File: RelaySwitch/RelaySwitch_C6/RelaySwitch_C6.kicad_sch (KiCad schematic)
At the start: 39 parts, among them J1 AC_MAINS_IN, J3 LOAD_CH1, J4 LOAD_CH2, J5 SW1_INPUT, J6 SW2_INPUT, K1 G5Q-1-DC5, K2 G5Q-1-DC5, Q1 MMBT8050, Q2 MMBT8050, U1 HLK-2M05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

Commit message: 07/03
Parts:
- removed R10: 1m, Resistor_SMD:R_2512_6332Metric, symbol Device:R
- added C2: 10u, Capacitor_SMD:C_0402_1005Metric, symbol Device:C_Small
- added C3: 100n, Capacitor_SMD:C_0402_1005Metric, symbol Device:C_Small
- R18: footprint Resistor_SMD:R_Shunt_Vishay_WSK2512_6332Metric_T2.66mm -> XIAO_Series_Footprints:RES_WSK2512R0100FEA; symbol Device:R -> WSK2512R0100FEA:WSK2512R0100FEA; Check_prices (none) -> https://www.snapeda.com/parts/WSK2512R0100FEA/Vishay/view-p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; Description_1 (none) -> Metal Strip Low Ohmic Smnt Resistor 2512 Case 10mOhm +/-1% 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; DigiKey_Part_Number (none) -> 541-WSK2512R0100FEACT-ND; MANUFACTURER (none) -> Vishay Dale; MAXIMUM_PACKAGE_HEIGHT (none) -> 0.889mm; MF (none) -> Vishay; MP (none) -> WSK2512R0100FEA; PARTREV (none) -> 04-Apr-2022; Package (none) -> None; SNAPEDA_PN (none) -> WSK2512R0100FEA; STANDARD (none) -> Manufacturer Recommendations; SnapEDA_Link (none) -> https://www.snapeda.com/parts/WSK2512R0100FEA/Vishay/view-p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
- U2: footprint XIAO_Series_Footprints:XIAO-ESP32-C6-SMD -> XIAO_Series_Footprints:XIAO-ESP32-C6-DIP
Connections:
- net +3V3: now also C3.1; no longer C5.1
- net +5V: now also C5.1, C2.1
- net GND: now also U5.4 (V2P), C2.2, C3.2; no longer U5.3 (V1N)
- net L: now also R18.I1; no longer R18.1, U5.4 (V2P)
- net L_Sense: now also R18.I2; no longer R18.2
- net at R13.2, R9.1, U5.2 (V1P): now also R18.E1
- new net: R18.E2, U5.3 (V1N)
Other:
- moved on the sheet: C5, C6

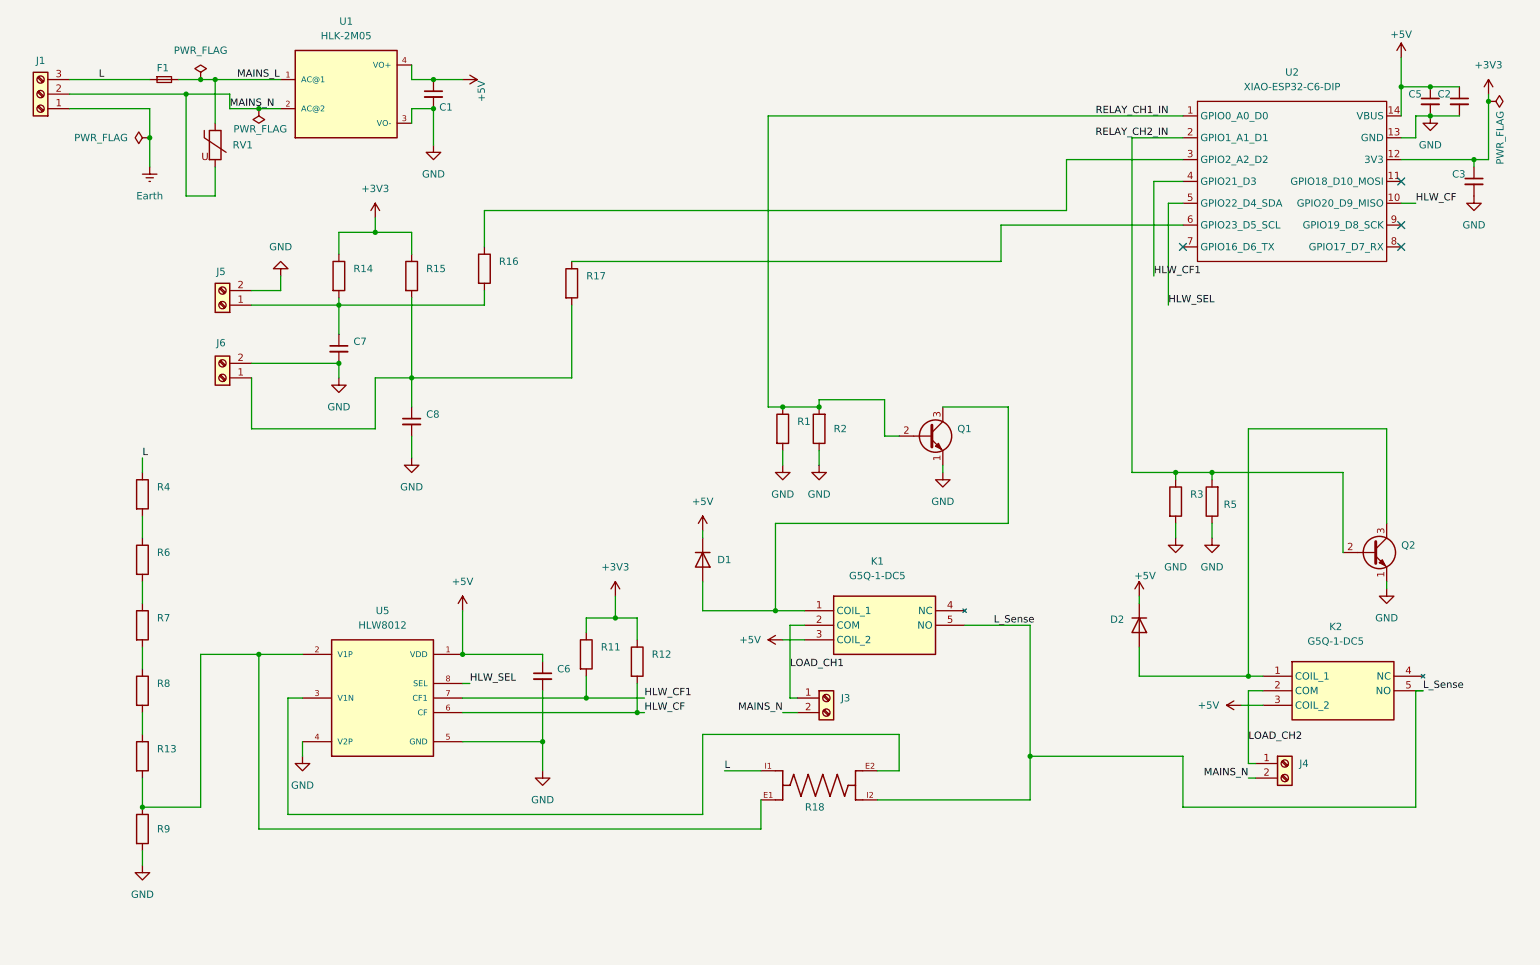
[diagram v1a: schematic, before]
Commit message: Reduced relay size
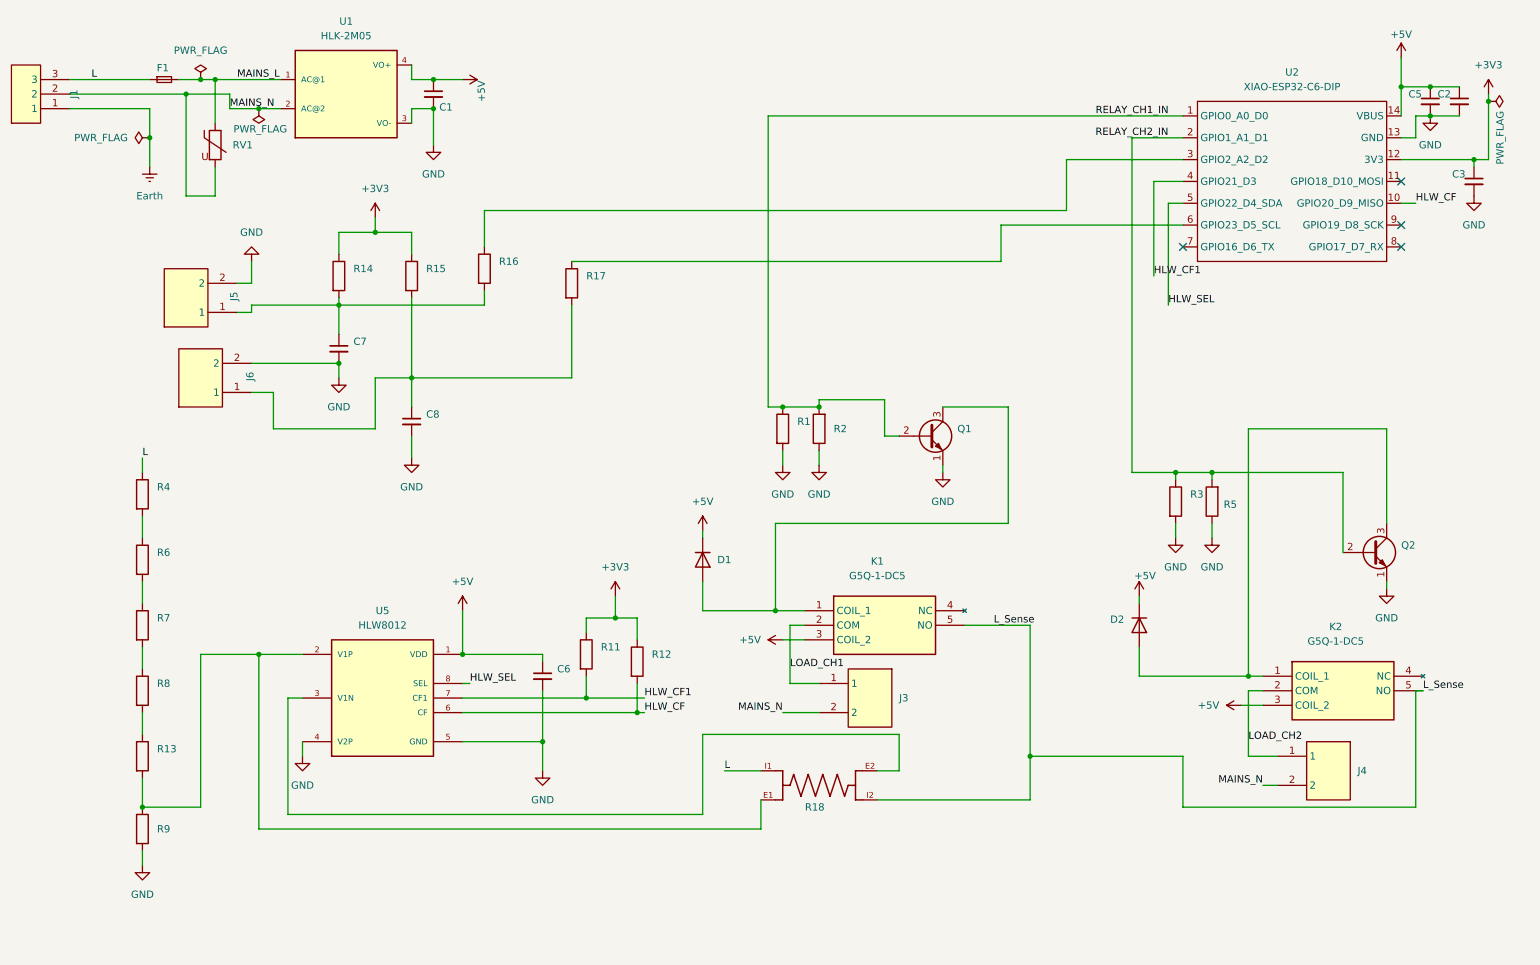
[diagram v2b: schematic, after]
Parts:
- J1: footprint TerminalBlock_Degson:TerminalBlock_Degson_DG250-3.5-03P_1x03_P3.50mm_45Degree -> seeed esp32:CONN-TH_3P-P5.00_WJ128V-5.0-3P; symbol Connector:Screw_Terminal_01x03 -> WJ128V3P:WJ128V-5.0-3P; Check_prices (none) -> https://www.snapeda.com/parts/TB0011-350-03BE/Same+Sky/view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; Description_1 (none) -> 3 Position Wire to Board Terminal Block Horizontal with Boa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; DigiKey_Part_Number (none) -> 2223-TB0011-350-03BE-ND; LCSC Part (none) -> C8270; MANUFACTURER (none) -> SAMESKY; MF (none) -> Same Sky; MP (none) -> TB0011-350-03BE; Package (none) -> None; SnapEDA_Link (none) -> https://www.snapeda.com/parts/TB0011-350-03BE/Same+Sky/view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
- J3, J4, J5, J6: footprint TerminalBlock_Degson:TerminalBlock_Degson_DG250-3.5-02P_1x02_P3.50mm_45Degree -> seeed esp32:CONN-TH_2P-P5.00_WJ128V-5.0-2P; symbol Connector:Screw_Terminal_01x02 -> WJ128V:WJ128V-5.0-2P; CREATOR (none) -> ASHISH; Check_prices (none) -> https://www.snapeda.com/parts/TB0011-350-02BE/Same+Sky/view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; Description_1 (none) -> 2 Position Wire to Board Terminal Block Horizontal with Boa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; DigiKey_Part_Number (none) -> 2223-TB0011-350-02BE-ND; LCSC Part (none) -> C8269; MANUFACTURER (none) -> Same Sky; MAXIMUM_PACKAGE_HEIGHT (none) -> 8.5mm; MF (none) -> Same Sky; MP (none) -> TB0011-350-02BE; PARTREV (none) -> 1.0; Package (none) -> None; STANDARD (none) -> Manufacturer Recommendations; SnapEDA_Link (none) -> https://www.snapeda.com/parts/TB0011-350-02BE/Same+Sky/view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
- U5: footprint HLW8012:SOIC8 -> seeed esp32:SOIC8

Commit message: For review
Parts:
- C2: footprint Capacitor_SMD:C_0402_1005Metric -> Capacitor_SMD:C_0805_2012Metric
- F1: value ~ -> T250mA/250V
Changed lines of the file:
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@@
 			)
 		)
-		(property "Footprint" "Capacitor_SMD:C_0402_1005Metric"
+		(property "Footprint" "Capacitor_SMD:C_0805_2012Metric"
 			(at 273.05 40.64 0)
 			(effects
@@
 			)
 		)
-		(property "Value" "~"
+		(property "Value" "T250mA/250V"
 			(at 46.99 34.29 0)
 			(effects

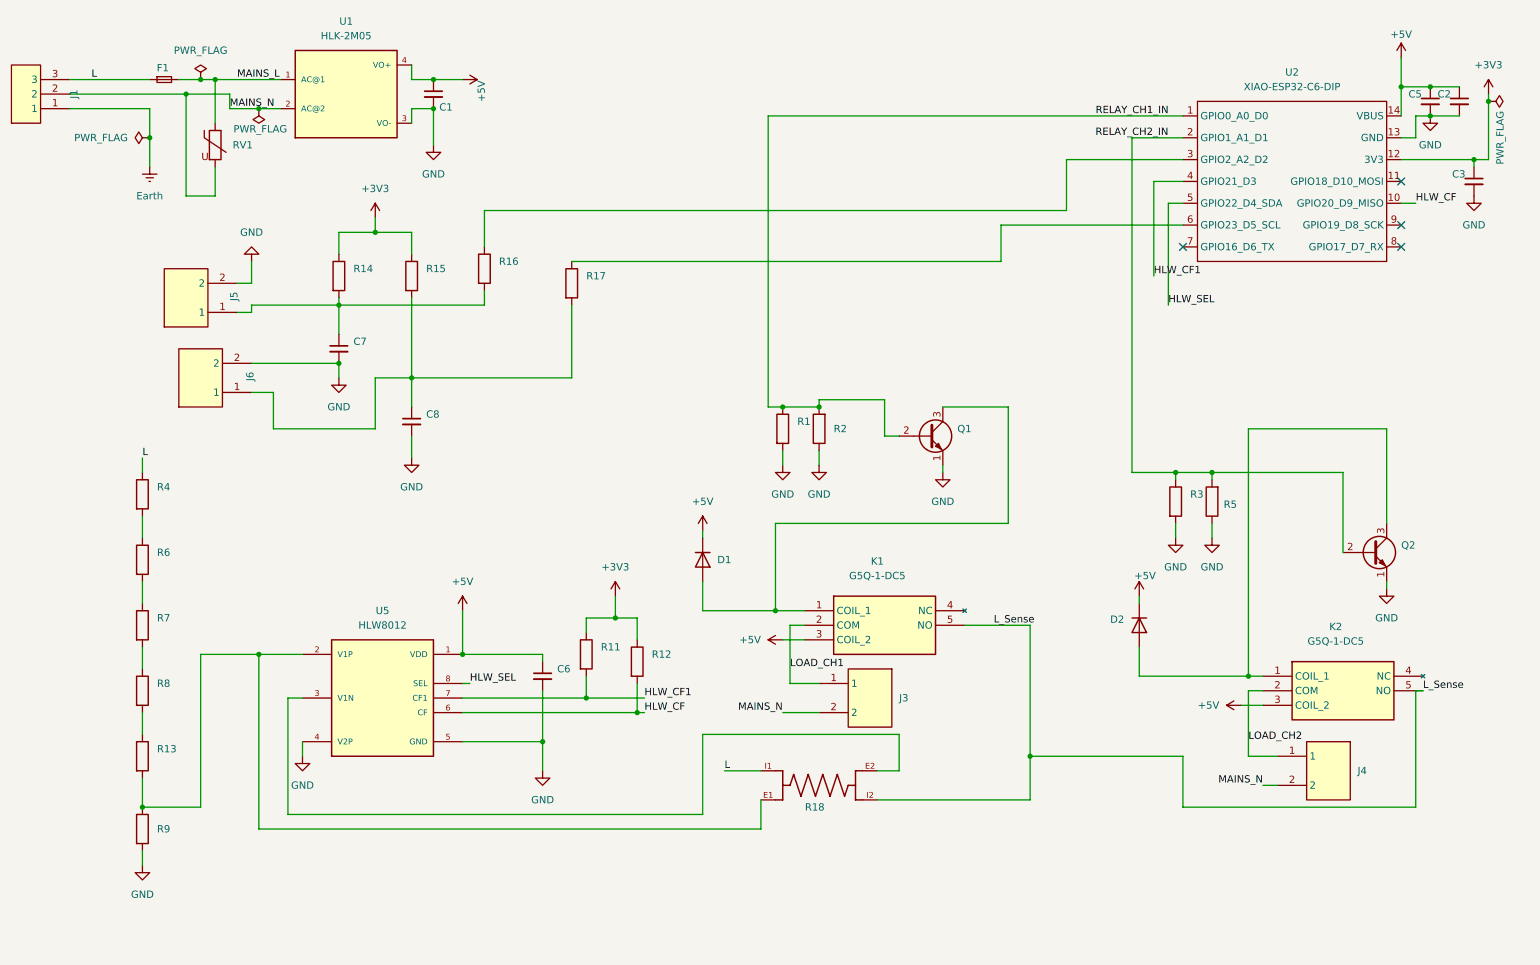
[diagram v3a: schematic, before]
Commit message: warning fix - 0  in schematic
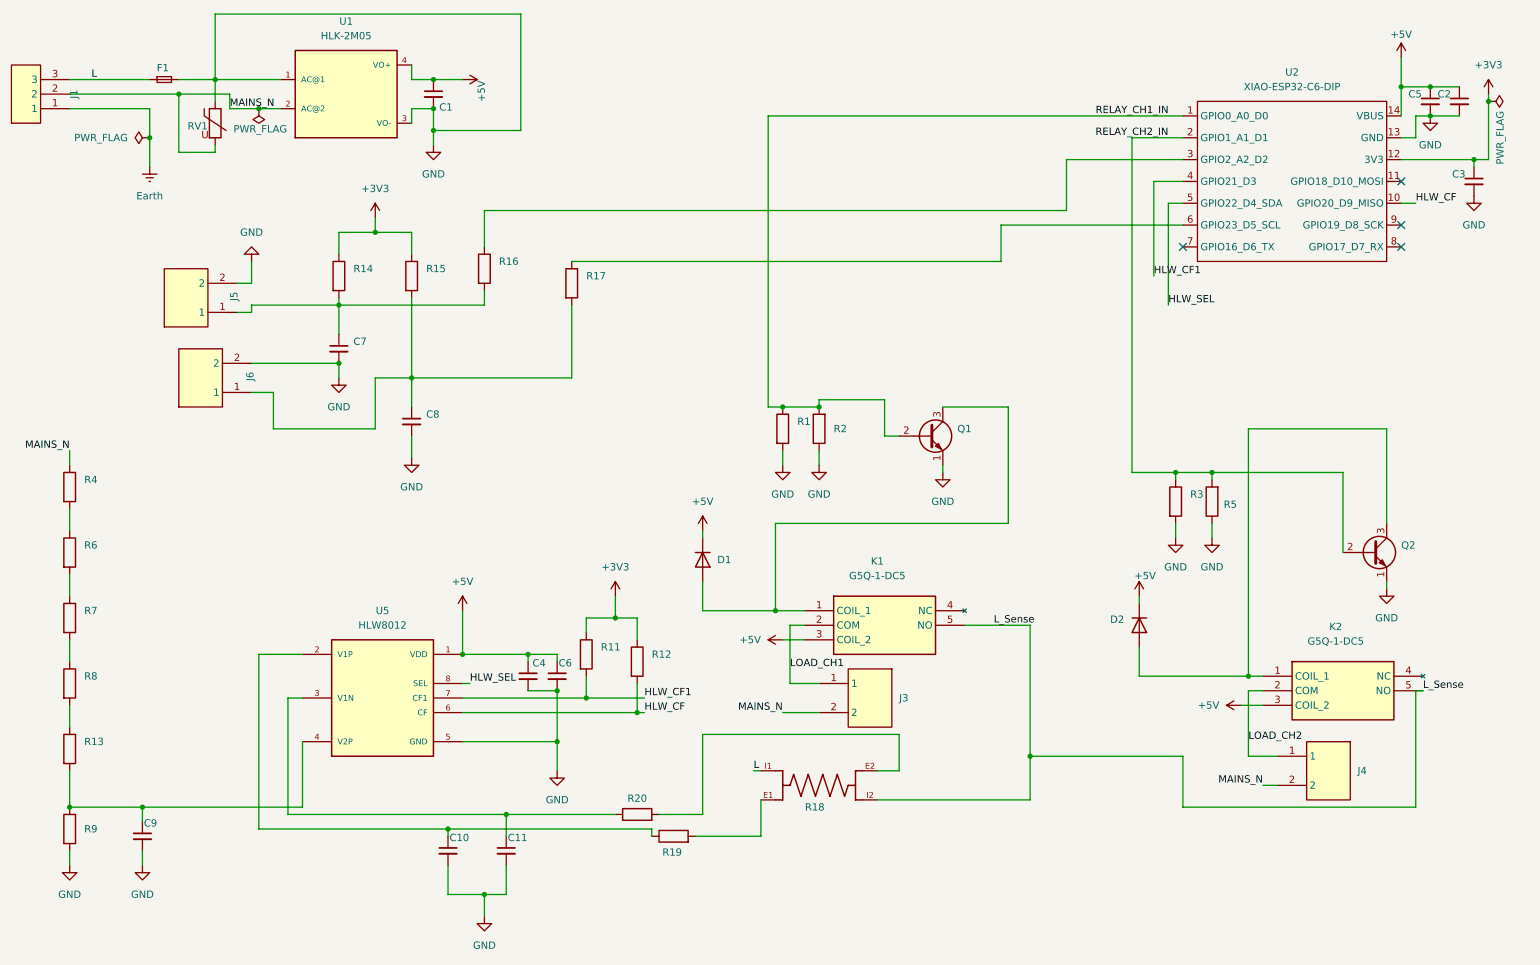
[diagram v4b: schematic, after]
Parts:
- added C10, C11, C9: 33n, Capacitor_SMD:C_0402_1005Metric, symbol Device:C_Small
- added C4: 0.1u, Capacitor_SMD:C_0402_1005Metric, symbol Device:C_Small
- added R19, R20: 1k, Resistor_SMD:R_0402_1005Metric, symbol Device:R
- C6: value 100n -> 10u
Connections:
- net MAINS_L is gone; now on net GND: F1.2, RV1.1, U1.1 (AC@1)
- net +5V: now also C4.1
- net GND: now also C10.2, C11.2, C4.2, C9.2; no longer U5.4 (V2P)
- net L: no longer R4.1
- net MAINS_N: now also R4.1
- net at R13.2, R9.1: now also U5.4 (V2P), C9.1; no longer R18.E1, U5.2 (V1P)
- net at U5.3 (V1N): now also C11.1, R20.1; no longer R18.E2
- new net: C10.1, R19.1, U5.2 (V1P)
- new net: R18.E2, R20.2
- new net: R18.E1, R19.2
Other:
- moved on the sheet: C6, R13, R4, R6, R7, R8, R9, RV1

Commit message: Fixed relay connections and F1 Fuse
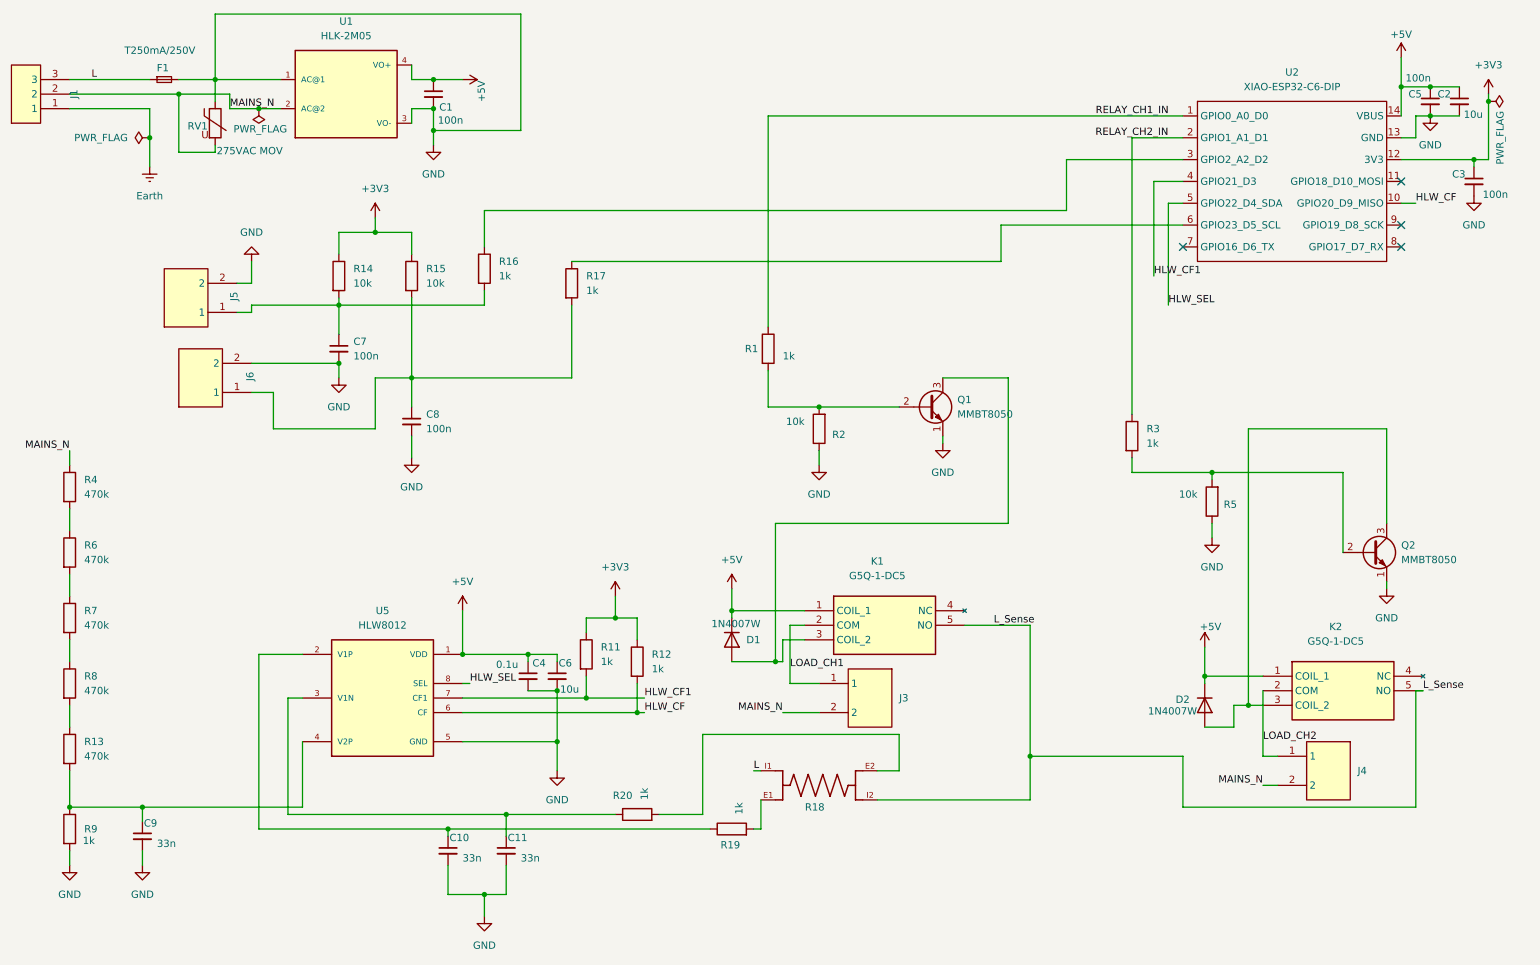
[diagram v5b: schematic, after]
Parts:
- F1: footprint Fuse:Fuse_1206_3216Metric -> Fuse:Fuseholder_Clip-5x20mm_Littelfuse_111_Inline_P20.00x5.00mm_D1.05mm_Horizontal
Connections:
- net +5V: now also K1.1 (COIL_1), K2.1 (COIL_1); no longer K1.3 (COIL_2), K2.3 (COIL_2)
- net GND: no longer R1.2, R3.2
- net RELAY_CH1_IN: no longer Q1.2 (B), R2.2
- net RELAY_CH2_IN: no longer Q2.2 (B), R5.2
- net at D1.2 (A), Q1.3 (C): now also K1.3 (COIL_2); no longer K1.1 (COIL_1)
- net at D2.2 (A), Q2.3 (C): now also K2.3 (COIL_2); no longer K2.1 (COIL_1)
- new net: Q1.2 (B), R1.2, R2.2
- new net: Q2.2 (B), R3.2, R5.2
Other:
- moved on the sheet: D1, D2, Q1, R1, R19, R3
